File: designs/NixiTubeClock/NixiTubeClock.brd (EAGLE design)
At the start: 160 x 100 mm, 14 parts, among them IC1 74141N, IC2 74141N, IC3 74141N, IC4 74141N

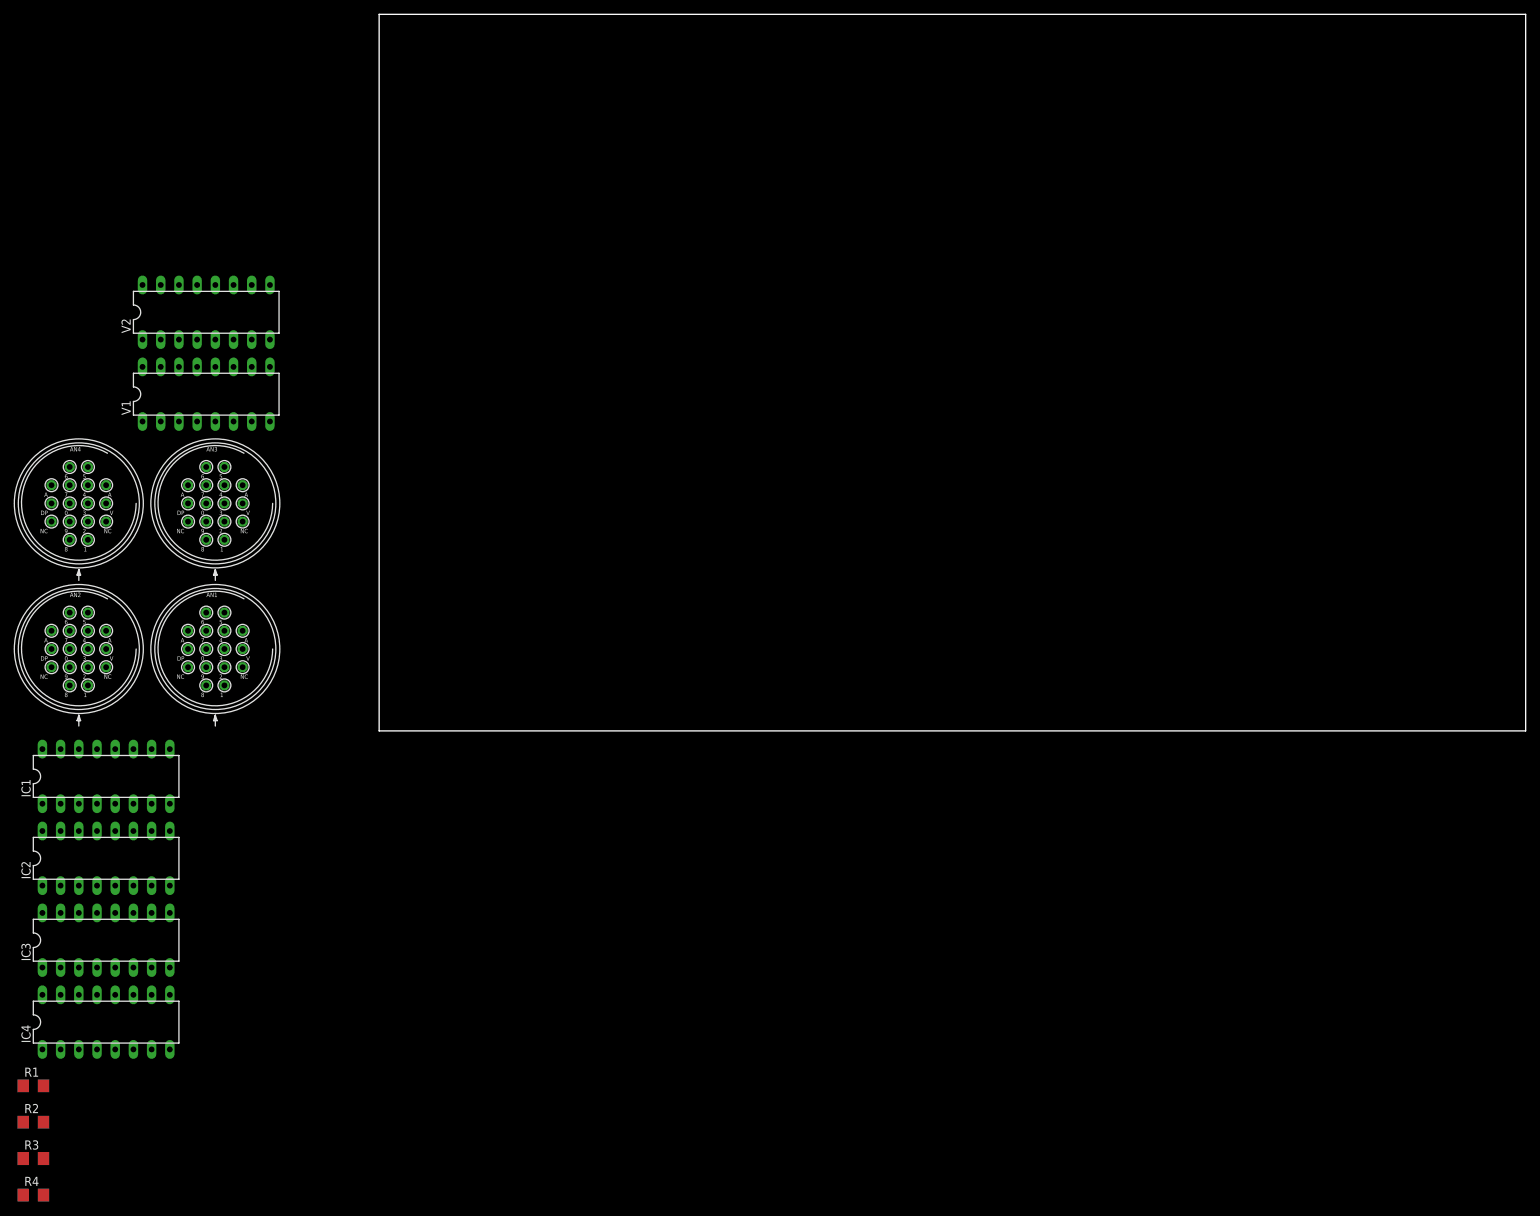
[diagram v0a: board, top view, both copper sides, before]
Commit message: added nixi tube project
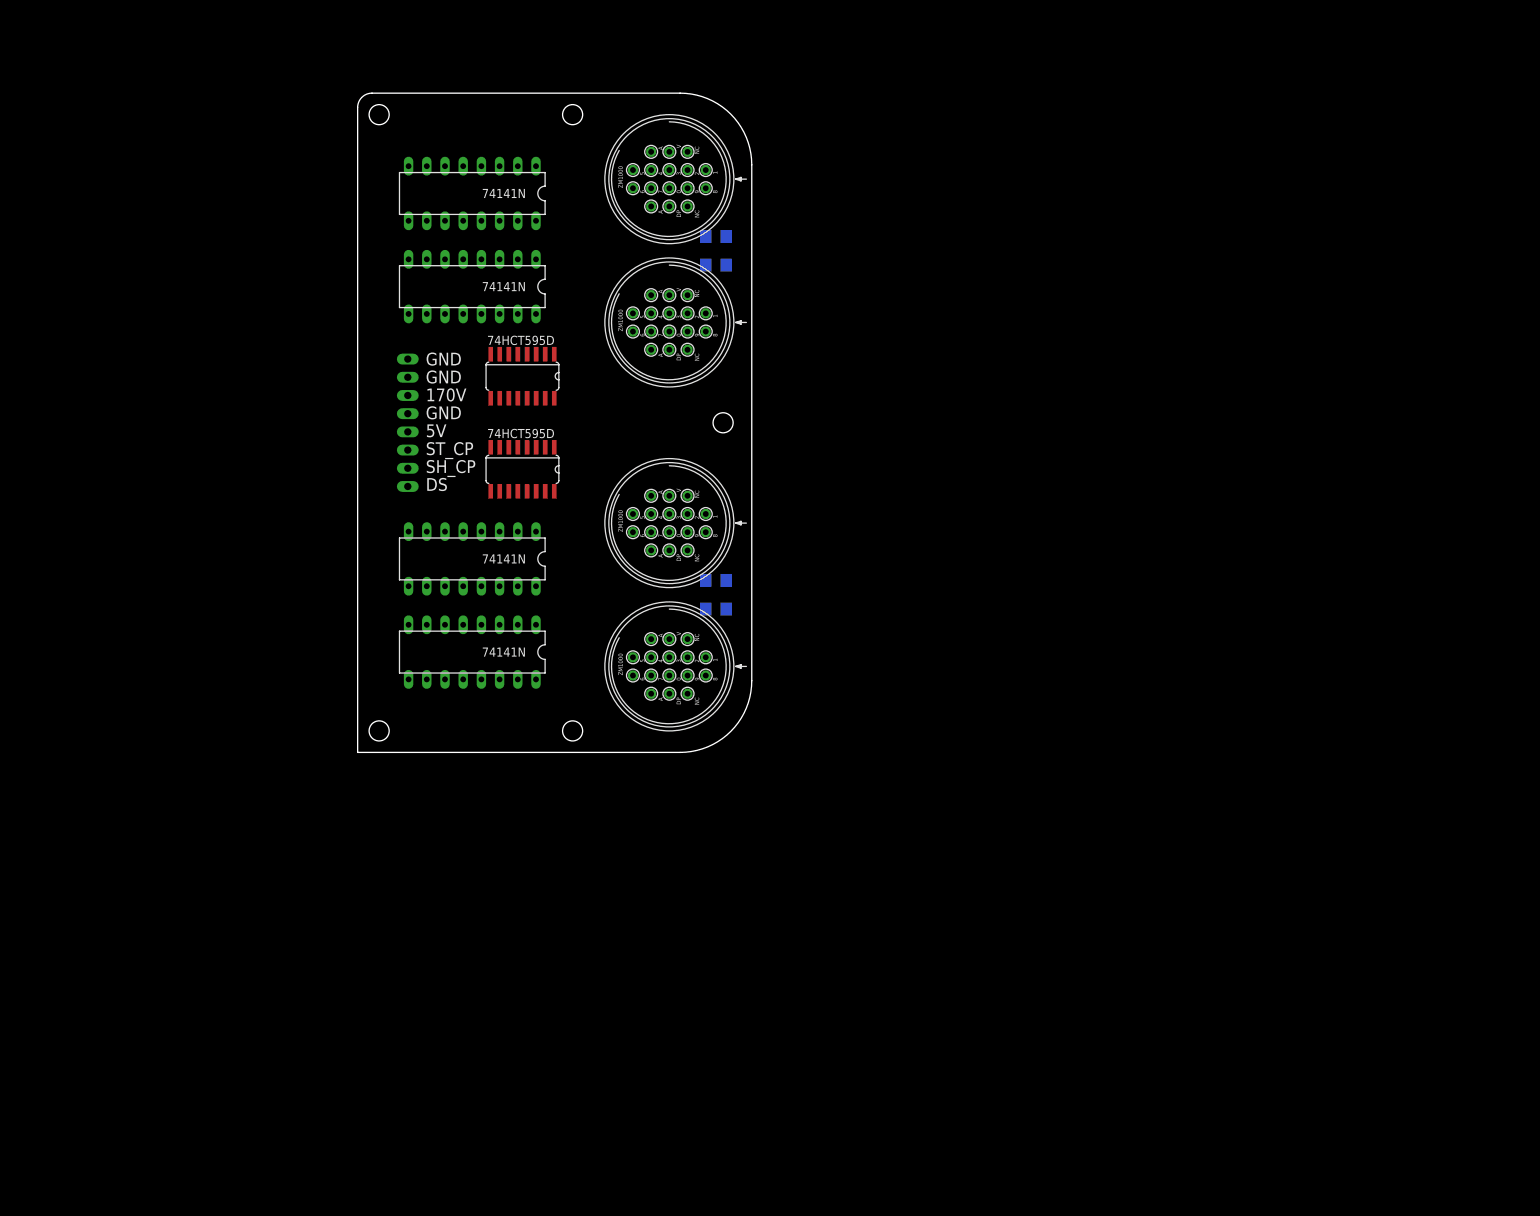
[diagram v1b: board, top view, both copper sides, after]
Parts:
- removed V1, V2: 74595N, NixieTube:DIL16
- added IC5: 74HCT595D, NixieTube:SO16
- added IC6: 74141N, NixieTube:DIL16
- added SV1: (no value), con-lstb:MA08-1
- IC2: value 74141N -> 74HCT595D; device NixieTube:DIL16 -> NixieTube:SO16
- R1, R2, R3: value (none) -> 12k
- R4: value 68Kh -> (none)
- moved R4 164.2 mm to (47.0, 69.0), flipped to the bottom, turned to 180 degrees
- moved R3 156.9 mm to (47.0, 65.0), flipped to the bottom, turned to 180 degrees
- moved R2 121.6 mm to (47.0, 21.0), flipped to the bottom, turned to 180 degrees
- moved R1 116.2 mm to (47.0, 17.0), flipped to the bottom, turned to 180 degrees
- moved IC4 114.7 mm to (13.0, 62.0), turned to 180 degrees
- moved AN2 105.3 mm to (40.5, 77.0), turned to 90 degrees
- moved AN4 85.5 mm to (40.5, 9.00), turned to 90 degrees
- moved IC2 79.5 mm to (20.0, 36.5), turned to 180 degrees
- moved AN1 78.0 mm to (40.5, 57.0), turned to 90 degrees
- moved IC3 73.8 mm to (13.0, 24.0), turned to 180 degrees
- moved AN3 63.4 mm to (40.5, 29.0), turned to 90 degrees
- moved IC1 54.0 mm to (13.0, 11.0), turned to 180 degrees
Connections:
- removed net +UB: V1.16, V2.16
- removed net -UB: V1.8, V2.8
- removed net N$1: IC2.4, V1.9
- removed net N$10: IC3.6, V2.7
- removed net N$11: IC3.7, V2.6
- removed net N$12: IC3.4, V2.5
- removed net N$14: IC4.6, V2.3
- removed net N$2: IC2.7, V1.7
- removed net N$3: IC2.6, V1.6
- removed net N$33: AN1.6, IC1.9
- removed net N$34: AN1.7, IC1.8
- removed net N$37: AN3.9, IC3.16
- removed net N$38: AN3.8, IC3.15
- removed net N$39: AN3.7, IC3.8
- removed net N$4: IC2.3, V1.5
- removed net N$40: AN3.6, IC3.9
- removed net N$41: AN3.5, IC3.13
- removed net N$42: AN3.4, IC3.14
- removed net N$43: AN3.3, IC3.11
- removed net N$44: AN3.2, IC3.10
- removed net N$45: AN3.1, IC3.1
- removed net N$46: AN3.0, IC3.2
- removed net N$47: AN4.9, IC4.16
- removed net N$48: AN4.8, IC4.15
- removed net N$49: AN4.7, IC4.8
- removed net N$5: IC1.4, V1.4
- removed net N$50: AN4.6, IC4.9
- removed net N$51: AN4.5, IC4.13
- removed net N$52: AN4.4, IC4.14
- removed net N$53: AN4.3, IC4.11
- removed net N$54: AN4.2, IC4.10
- removed net N$55: AN4.1, IC4.1
- removed net N$56: AN4.0, IC4.2
- removed net N$6: IC1.7, V1.3
- removed net N$8: IC1.3, V1.1
- new net 170V: R1.2, R2.2, R3.2, R4.2, SV1.6
- new net DS: IC2.14, SV1.1
- new net N$100: AN4.A, R4.1
- new net N$101: IC1.3, IC2.15
- new net N$102: IC1.6, IC2.1
- new net N$103: IC1.7, IC2.2
- new net N$104: IC1.4, IC2.3
- new net N$105: IC2.4, IC3.3
- new net N$106: IC2.5, IC3.6
- new net N$107: IC2.6, IC3.7
- new net N$108: IC2.7, IC3.4
- new net N$109: IC4.3, IC5.15
- new net N$110: IC4.6, IC5.1
- new net N$111: IC4.7, IC5.2
- new net N$112: IC5.3
- new net N$113: IC5.4, IC6.3
- new net N$114: IC5.5, IC6.6
- new net N$115: IC5.6, IC6.7
- new net N$116: IC5.7, IC6.4
- new net N$66: AN3.3, IC4.9
- new net N$67: AN3.4, IC4.13
- new net N$68: AN3.5, IC4.14
- new net N$69: AN3.6, IC4.11
- new net N$70: AN3.7, IC4.10
- new net N$71: AN3.8, IC4.1
- new net N$72: AN3.9, IC4.2
- new net N$73: AN4.0, IC6.16
- new net N$74: AN4.1, IC6.15
- new net N$75: AN4.2, IC6.8
- new net N$76: AN4.3, IC6.9
- new net N$91: AN4.4, IC6.13
- new net N$92: AN4.5, IC6.14
- new net N$93: AN4.6, IC6.11
- new net N$94: AN4.7, IC6.10
- new net N$95: AN4.8, IC6.1
- new net N$96: AN4.9, IC6.2
- new net N$97: AN1.A, R1.1
- new net N$98: AN2.A, R2.1
- new net N$99: AN3.A, R3.1
- new net SHIFT_DATA: IC2.9, IC5.14
- new net SH_CP: IC2.11, IC5.11, SV1.2
- new net ST_CP: IC2.12, IC5.12, SV1.3
- new net VCC: IC1.5, IC2.16, IC3.5, IC4.5, IC5.16, IC6.5, SV1.4
- net 5V: now also IC2.10, IC5.10; no longer IC1.5, IC2.5, IC3.5, IC4.5
- net GND: now also IC2.13, IC2.8, IC5.13, IC5.8, IC6.12, SV1.5, SV1.7, SV1.8; no longer IC2.12
- net N$13: now also AN1.2, IC1.8; no longer IC4.3, V2.4
- net N$15: now also AN1.3, IC1.9; no longer IC4.7, V2.2
- net N$16: now also AN1.4, IC1.13; no longer IC4.4, V2.1
- net N$17: now also AN1.5, IC1.14; no longer AN2.9, IC2.16
- net N$18: now also AN1.6, IC1.11; no longer AN2.8, IC2.15
- net N$19: now also AN1.7, IC1.10; no longer AN2.7, IC2.8
- net N$20: now also AN1.8, IC1.1; no longer AN2.6, IC2.9
- net N$21: now also AN1.9, IC1.2; no longer AN2.5, IC2.13
- net N$22: now also AN2.0, IC3.16; no longer AN2.4, IC2.14
- net N$23: now also AN2.1, IC3.15; no longer AN2.3, IC2.11
- net N$24: now also IC3.8; no longer IC2.10
- net N$25: now also AN2.3, IC3.9; no longer AN2.1, IC2.1
- net N$26: now also AN2.4, IC3.13; no longer AN2.0, IC2.2
- net N$27: now also AN2.5, IC3.14; no longer AN1.0, IC1.2
- net N$28: now also AN2.6, IC3.11; no longer AN1.1, IC1.1
- net N$29: now also AN2.7, IC3.10; no longer AN1.2, IC1.10
- net N$30: now also AN2.8, IC3.1; no longer AN1.3, IC1.11
- net N$31: now also AN2.9, IC3.2; no longer AN1.4, IC1.14
- net N$32: now also AN3.0, IC4.16; no longer AN1.5, IC1.13
- net N$35: now also AN3.1, IC4.15; no longer AN1.8, IC1.15
- net N$36: now also AN3.2, IC4.8; no longer AN1.9, IC1.16
- net N$7: now also AN1.0, IC1.16; no longer IC1.6, V1.2
- net N$9: now also AN1.1, IC1.15; no longer IC3.3, V2.9
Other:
- board size 160 x 100 mm -> 55 x 92 mm
- board text added: "170V"
- board text added: "5V"
- board text added: "DS"
- board text added: "GND"
- board text added: "SH_CP"
- board text added: "ST_CP"

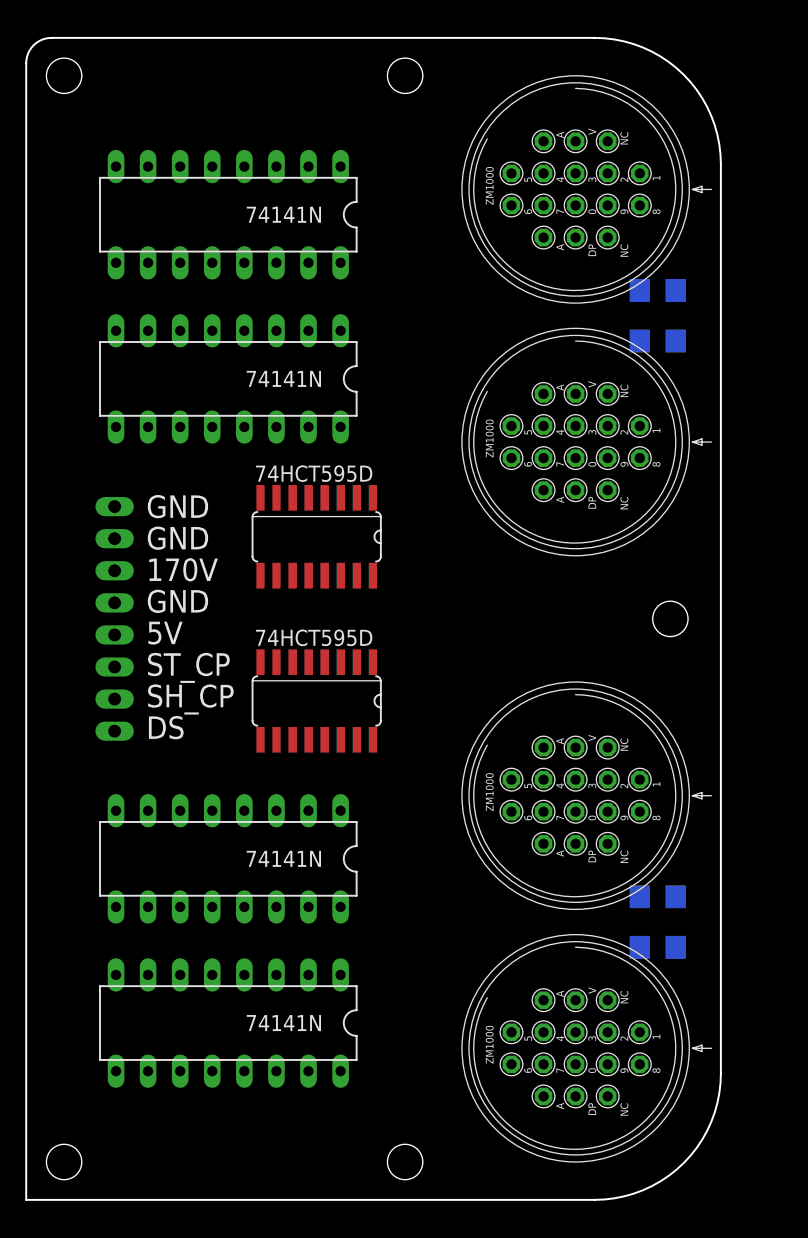
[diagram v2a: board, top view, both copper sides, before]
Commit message: added parts for nixi clock final check during the week
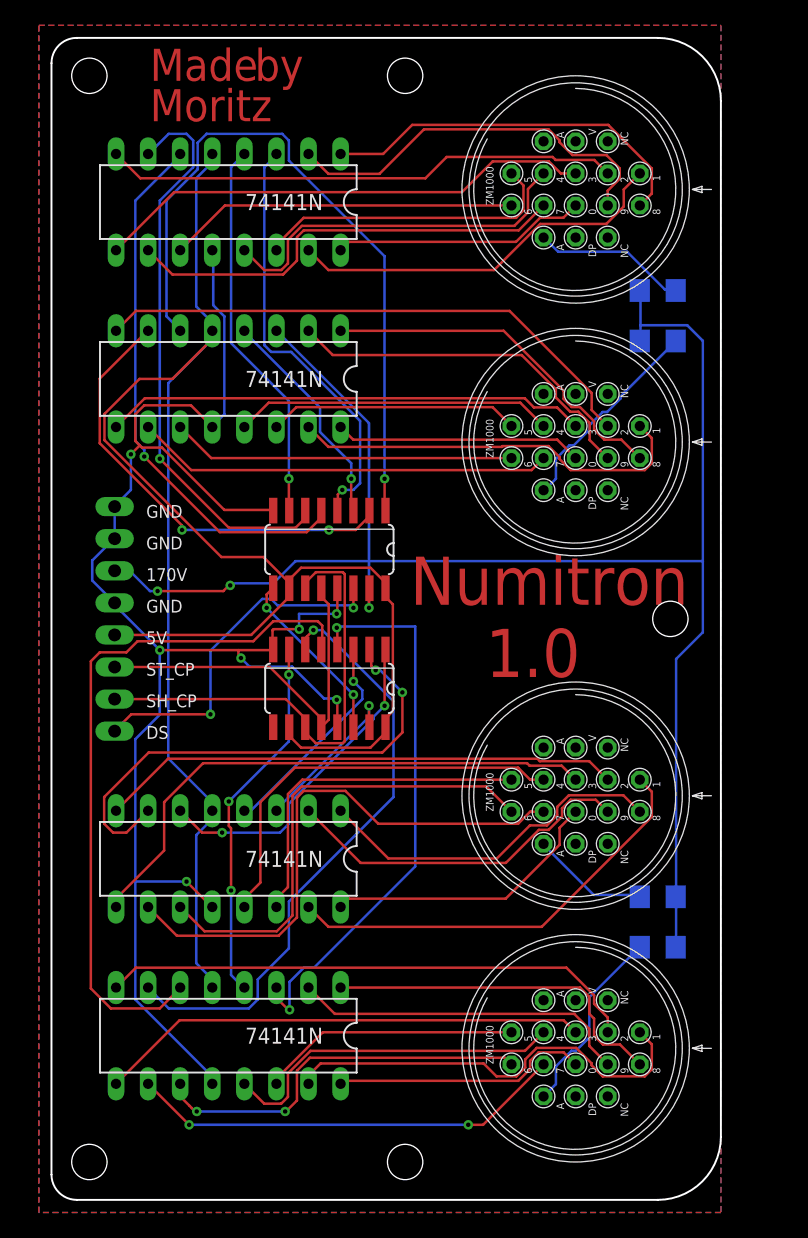
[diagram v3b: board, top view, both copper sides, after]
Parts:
- R4: value (none) -> 12k
- moved IC6 65.0 mm to (13.0, 10.0)
- moved IC3 52.0 mm to (13.0, 76.0)
- moved R1 52.0 mm to (47.0, 69.0), turned to 0 degrees
- moved R4 52.0 mm to (47.0, 17.0)
- moved IC1 51.0 mm to (13.0, 62.0)
- moved R2 44.0 mm to (47.0, 65.0), turned to 0 degrees
- moved R3 44.0 mm to (47.0, 21.0)
- moved IC4 38.0 mm to (13.0, 24.0)
- moved IC2 12.0 mm to (21.0, 48.5)
- moved IC5 12.0 mm to (21.0, 37.5)
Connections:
- removed net N$112: IC5.3
- removed net VCC: IC1.5, IC2.16, IC3.5, IC4.5, IC5.16, IC6.5, SV1.4
- new net N$1: IC4.4, IC5.3
- net 5V: now also IC1.5, IC2.16, IC3.5, IC4.5, IC5.16, IC6.5, SV1.4
- net N$97: now also R2.1; no longer R1.1
- net N$98: now also R1.1; no longer R2.1
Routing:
- net 5V: track 0.00 -> 150.9 mm
- net GND: track 0.00 -> 133.0 mm, vias 0 -> 7
- net 170V: track 0.00 -> 106.7 mm, vias 0 -> 2
- net N$102: track 0.00 -> 56.6 mm, vias 0 -> 1
- net N$114: track 0.00 -> 56.0 mm
- net N$115: track 0.00 -> 48.2 mm, vias 0 -> 1
- net N$113: track 0.00 -> 46.4 mm, vias 0 -> 2
- net N$107: track 0.00 -> 45.4 mm, vias 0 -> 1
- net N$66: track 0.00 -> 44.3 mm
- net N$13: track 0.00 -> 44.1 mm
- net N$70: track 0.00 -> 44.0 mm
- net N$106: track 0.00 -> 43.2 mm, vias 0 -> 1
- net N$75: track 0.00 -> 42.8 mm
- net N$36: track 0.00 -> 41.3 mm
- net N$24: track 0.00 -> 41.0 mm
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- added copper zone on layer 1, net GND
- added copper zone on layer 16, net GND
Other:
- board size 55 x 92 mm -> 53 x 92 mm
- board text added: "Made"
- board text added: "Moritz"
- board text added: "Numitron 1.0"
- board text added: "by"
